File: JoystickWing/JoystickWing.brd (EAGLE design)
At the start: 32.7 x 69.8 mm, 14 parts, among them J1 5747844-4

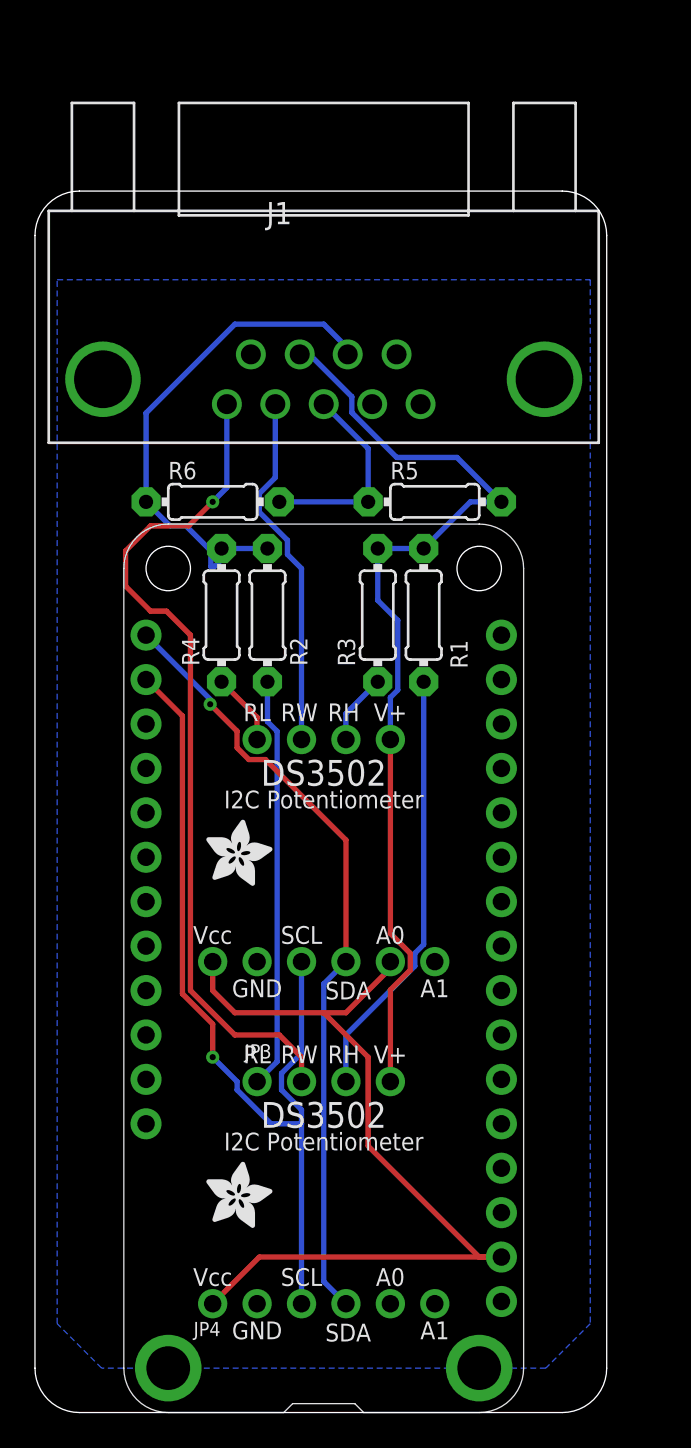
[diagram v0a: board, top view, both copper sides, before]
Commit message: Added NeoPixel w/jumper & pin
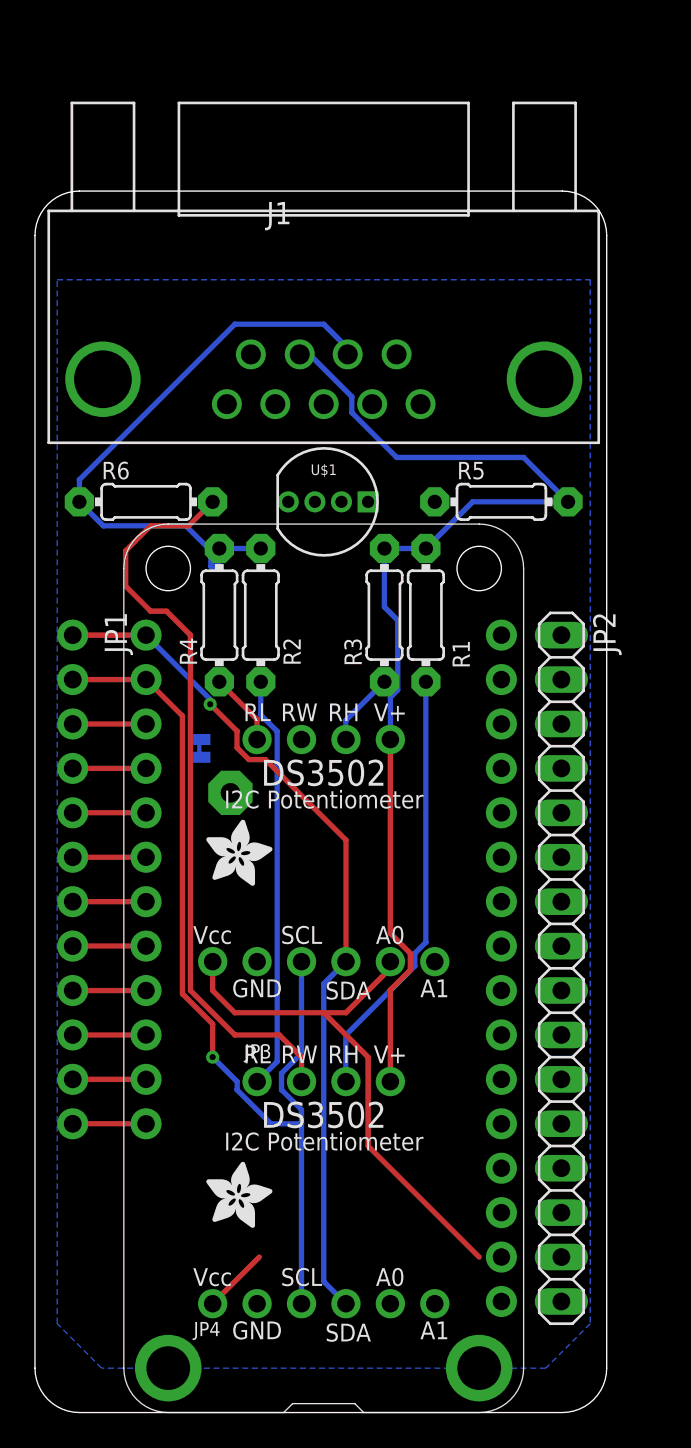
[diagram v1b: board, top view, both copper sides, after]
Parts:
- added JP1: (no value), adafruit:1X12-CB
- added JP2: (no value), pinhead:1X16
- added JP7: JUMPER-SMT_2_NC_TRACE_SILK, SparkFun-Jumpers:SMT-JUMPER_2_NC_TRACE_SILK
- added PAD1: (no value), wirepad:2,54/1,1
- added U$1: NEOPIXELS-5MM, milador:NEOPIXELS-5MM
- moved R5 3.81 mm to (26.7, 52.1)
- moved R6 3.81 mm to (6.35, 52.1)
- moved R2 0.38 mm to (12.9, 45.6)
- moved R3 0.38 mm to (20.0, 45.6)
- moved R1 0.13 mm to (22.4, 45.6)
- moved R4 0.13 mm to (10.5, 45.6)
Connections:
- new net N$1: JP1.3, JP7.1, MS1.19
- new net N$10: JP2.1, MS1.16
- new net N$11: JP2.2, MS1.15
- new net N$12: JP2.3, MS1.14
- new net N$13: JP2.4, MS1.13
- new net N$14: JP2.5, MS1.12
- new net N$15: JP2.6, MS1.11
- new net N$16: JP2.7, MS1.10
- new net N$17: JP2.8, MS1.9
- new net N$18: JP2.9, MS1.8
- new net N$19: JP2.10, MS1.7
- new net N$2: JP1.4, MS1.20
- new net N$20: JP2.11, MS1.6
- new net N$21: JP2.12, MS1.5
- new net N$22: JP2.13, MS1.4
- new net N$23: JP2.14, MS1.3
- new net N$24: JP2.16, MS1.1
- new net N$25: JP7.2, PAD1.1, U$1.1
- new net N$3: JP1.5, MS1.21
- new net N$4: JP1.6, MS1.22
- new net N$5: JP1.7, MS1.23
- new net N$6: JP1.8, MS1.24
- new net N$8: JP1.9, MS1.25
- new net N$9: JP1.11, MS1.27
- new net USB: JP1.10, MS1.26
- new net VBAT: JP1.12, MS1.28
- net GND: now also U$1.3; no longer MS1.4
- net SCL: now also JP1.2
- net SDA: now also JP1.1
- net VCC: now also JP2.15, U$1.2
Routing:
- net P2RW: track 20.6 -> 0.00 mm
- net VCC: track 50.3 -> 35.2 mm
- net N$7: track 11.7 -> 0.00 mm
- net +12V: track 55.8 -> 62.9 mm
- net P1RW: track 48.6 -> 42.7 mm
- net GND: track 29.2 -> 34.2 mm
- net SDA: track 44.6 -> 48.8 mm
- net SCL: track 50.6 -> 54.8 mm
- net VBAT: track 0.00 -> 4.19 mm
- net USB: track 0.00 -> 4.19 mm
- net N$9: track 0.00 -> 4.19 mm
- net N$8: track 0.00 -> 4.19 mm
- net N$6: track 0.00 -> 4.19 mm
- net N$5: track 0.00 -> 4.19 mm
- net N$4: track 0.00 -> 4.19 mm
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
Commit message: Updated to add neopixel & jumper - no air wires
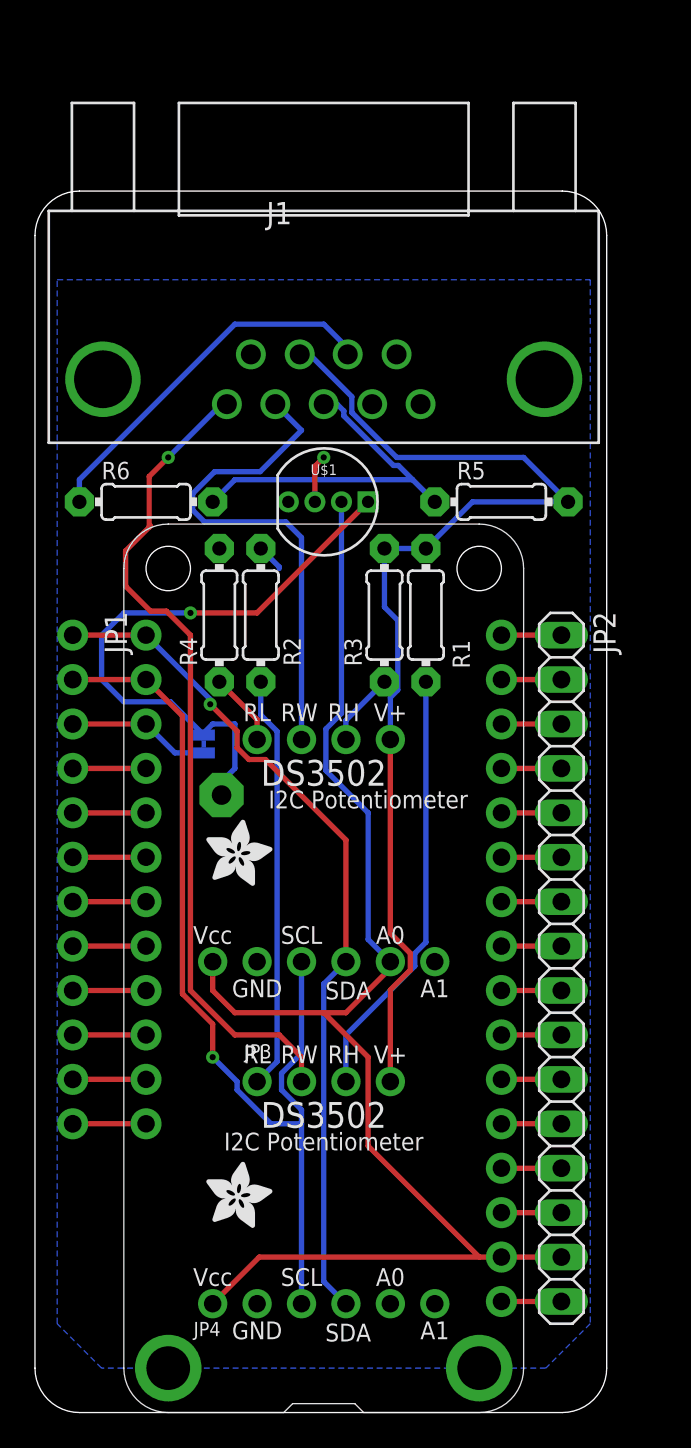
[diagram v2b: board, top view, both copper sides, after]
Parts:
- moved PAD1 0.52 mm to (10.7, 35.3)
- moved JP7 0.36 mm to (9.65, 38.2), turned to 90 degrees
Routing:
- net VCC: track 35.2 -> 80.6 mm
- net N$25: track 0.00 -> 34.6 mm, vias 0 -> 1
- net P2RW: track 0.00 -> 29.2 mm
- net N$7: track 0.00 -> 20.8 mm
- net GND: track 34.2 -> 25.5 mm, vias 0 -> 1
- net P1RW: track 42.7 -> 47.6 mm
- net N$1: track 4.19 -> 8.18 mm
- net N$18: track 0.00 -> 3.81 mm
- net N$17: track 0.00 -> 3.81 mm
- net N$24: track 0.00 -> 3.43 mm
- net N$23: track 0.00 -> 3.43 mm
- net N$22: track 0.00 -> 3.43 mm
- net N$21: track 0.00 -> 3.43 mm
- net N$20: track 0.00 -> 3.43 mm
- net N$19: track 0.00 -> 3.43 mm
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
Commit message: Added User Switch Output
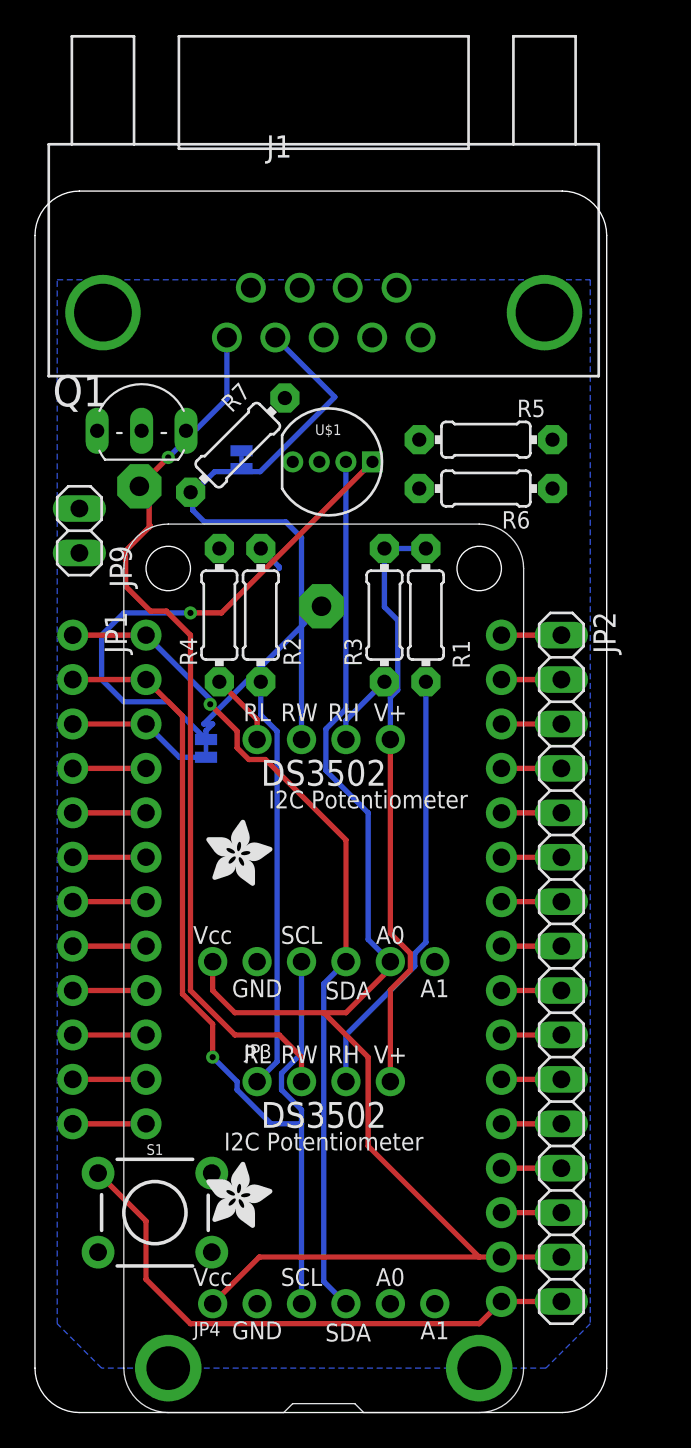
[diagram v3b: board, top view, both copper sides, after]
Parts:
- added JP8: JUMPER-SMT_2_NC_TRACE_SILK, SparkFun-Jumpers:SMT-JUMPER_2_NC_TRACE_SILK
- added JP9: (no value), pinhead:1X02
- added PAD2: (no value), wirepad:2,54/1,1
- added Q1: 2N2222, adafruit:TO92-EBC-OVAL
- added R7: 1K, adafruit:0204/7
- added S1: MOMENTARY-SWITCH-SPST-PTH-6.0MM, SparkFun-Switches:TACTILE_SWITCH_PTH_6.0MM
- moved R6 19.4 mm to (25.8, 52.8), turned to 180 degrees
- moved PAD1 12.2 mm to (16.4, 46.1)
- moved J1 3.81 mm to (16.5, 72.4)
- moved R5 3.67 mm to (25.8, 55.6)
- moved U$1 2.30 mm to (17.0, 54.4)
- moved JP7 0.28 mm to (9.78, 38.0)
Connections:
- removed net N$22: JP2.13, MS1.4
- new net N$26: Q1.B, R7.1
- new net N$27: JP9.1, Q1.E
- new net N$28: JP8.2, PAD2.1, R7.2
- net GND: now also JP2.13, JP9.2, MS1.4, S1.3
- net N$2: now also JP8.1
- net N$24: now also S1.1
- net N$7: now also Q1.C
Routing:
- net N$24: track 3.43 -> 32.5 mm
- net +12V: track 62.9 -> 34.3 mm
- net N$7: track 20.8 -> 0.00 mm
- net GND: track 25.5 -> 5.01 mm, vias 1 -> 0
- net N$25: track 34.6 -> 40.6 mm
- net P2RW: track 29.2 -> 34.6 mm
- net P1RW: track 47.6 -> 51.2 mm
- net N$22: track 3.43 -> 0.00 mm
- net VCC: track 80.6 -> 83.0 mm

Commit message: Removed transistor
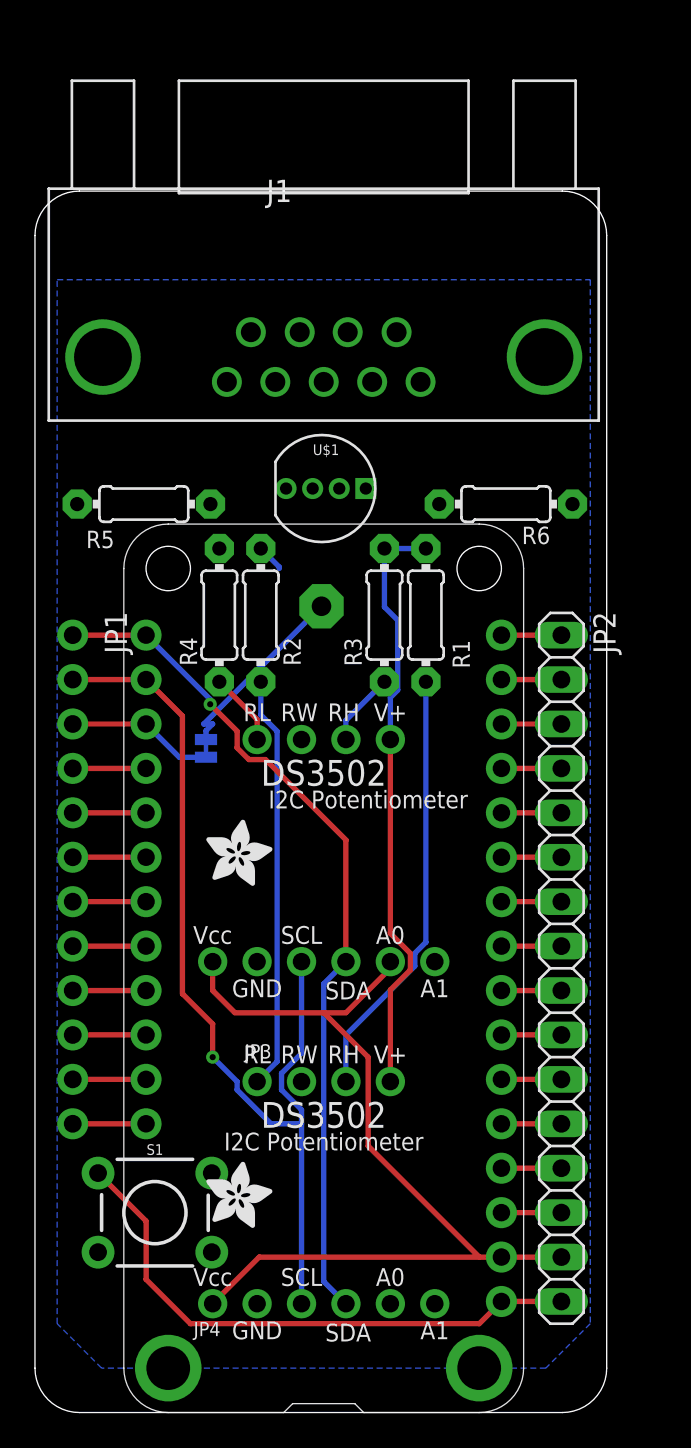
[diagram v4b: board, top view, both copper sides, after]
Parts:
- removed JP8: JUMPER-SMT_2_NC_TRACE_SILK, SparkFun-Jumpers:SMT-JUMPER_2_NC_TRACE_SILK
- removed JP9: (no value), pinhead:1X02
- removed PAD2: (no value), wirepad:2,54/1,1
- removed Q1: 2N2222, adafruit:TO92-EBC-OVAL
- removed R7: 1K, adafruit:0204/7
- moved R5 19.9 mm to (6.22, 51.9)
- moved J1 2.54 mm to (16.5, 69.8)
- moved U$1 1.57 mm to (16.6, 52.8)
- moved R6 1.45 mm to (26.9, 51.9)
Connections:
- removed net N$26: Q1.B, R7.1
- removed net N$27: JP9.1, Q1.E
- removed net N$28: JP8.2, PAD2.1, R7.2
- net GND: no longer JP9.2
- net N$2: no longer JP8.1
- net N$7: no longer Q1.C
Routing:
- net P1RW: track 51.2 -> 0.00 mm, vias 1 -> 0
- net P2RW: track 34.6 -> 0.00 mm
- net VCC: track 83.0 -> 52.5 mm
- net N$25: track 40.6 -> 11.1 mm, vias 1 -> 0

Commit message: No AirWires & ready for reset button and double check
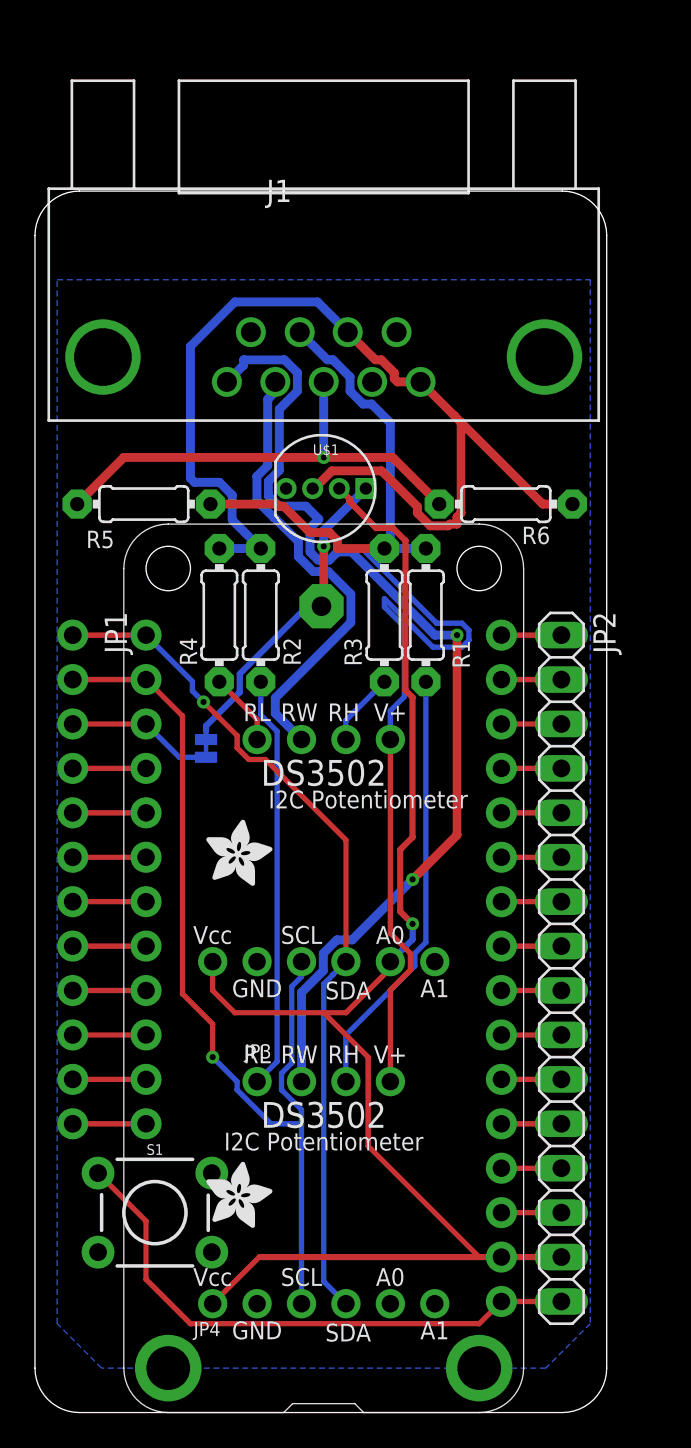
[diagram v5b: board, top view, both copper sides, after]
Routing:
- net GND: track 5.01 -> 63.8 mm
- net P1RW: track 0.00 -> 58.8 mm, vias 0 -> 2
- net +12V: track 34.3 -> 74.2 mm
- net VCC: track 52.5 -> 82.9 mm, vias 0 -> 1
- net N$7: track 0.00 -> 27.2 mm, vias 0 -> 1
- net P2RW: track 0.00 -> 26.0 mm
- net N$25: track 11.1 -> 18.6 mm, vias 0 -> 1

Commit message: Update with address pads
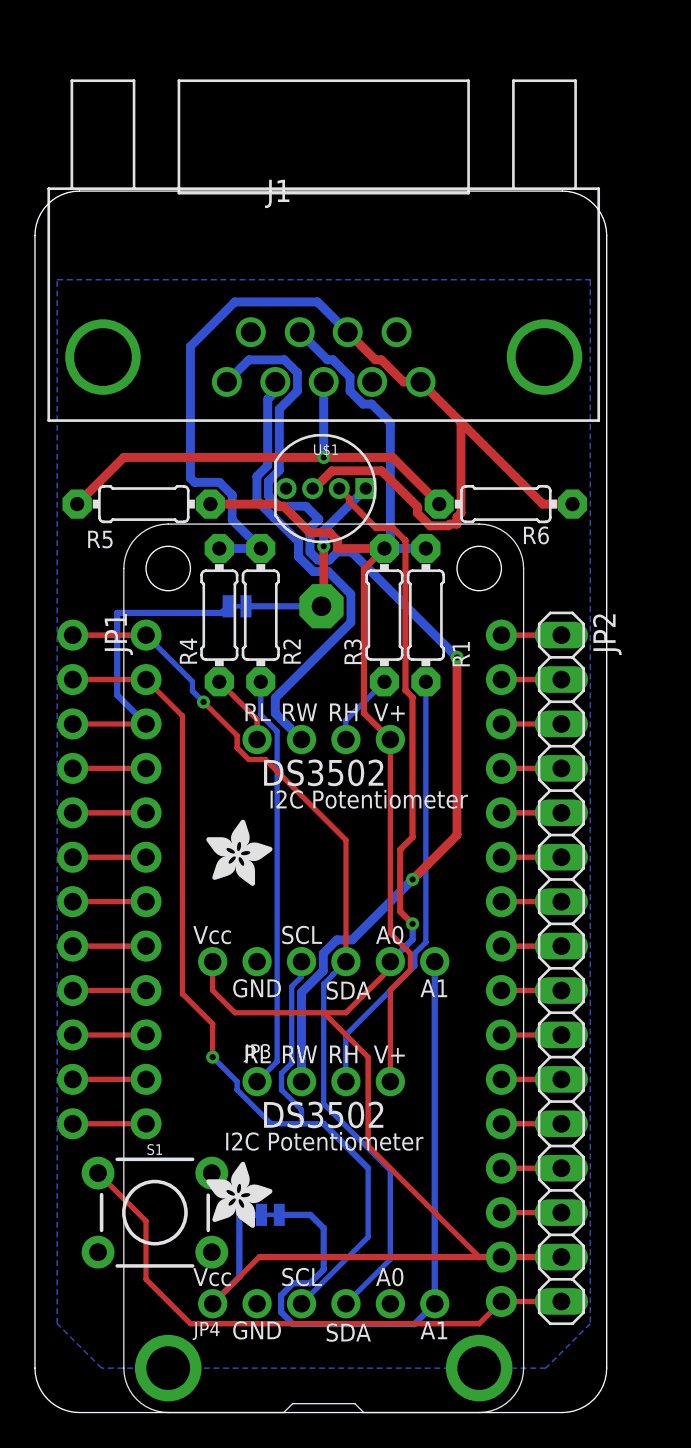
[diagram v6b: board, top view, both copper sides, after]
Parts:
- added A1: JUMPER-SMT_2_NC_TRACE_SILK, SparkFun-Jumpers:SMT-JUMPER_2_NC_TRACE_SILK
- moved JP7 8.32 mm to (11.6, 46.1), turned to 180 degrees
- renumbered PAD1 to NEOPIN
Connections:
- removed net P1A1: JP4.6
- removed net P2A1: JP6.6
- new net ADDR: A1.1, JP4.6, JP6.6
- net VCC: now also A1.2
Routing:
- net ADDR: track 0.00 -> 38.6 mm
- net +12V: track 74.2 -> 61.3 mm
- net N$1: track 8.41 -> 17.7 mm
- net VCC: track 82.9 -> 89.9 mm
- net N$25: track 18.6 -> 12.1 mm
- net SCL: track 54.8 -> 58.7 mm
- net SDA: track 48.8 -> 50.9 mm
- net P1RW: track 58.8 -> 57.8 mm
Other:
- board text added: "3V"
- board text added: "JoyStick"
- board text added: "Uncut = 1 Cut = 0"

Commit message: Added the missing Neopixel led pads and updated the switch to DTS-3: 3.5x6mm style switch.
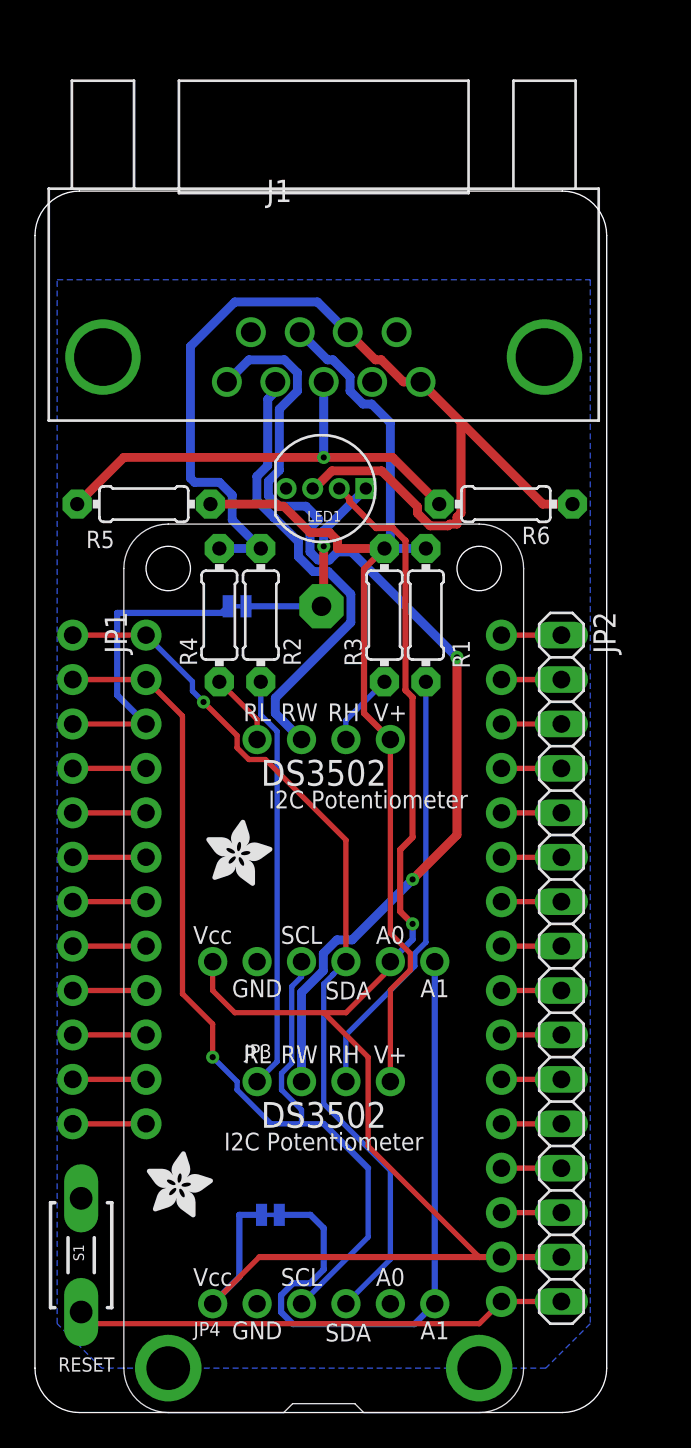
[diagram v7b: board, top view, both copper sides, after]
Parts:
- S1: value MOMENTARY-SWITCH-SPST-PTH-6.0MM -> RESET; device SparkFun-Switches:TACTILE_SWITCH_PTH_6.0MM -> milador:DTS-3
- moved S1 4.87 mm to (2.64, 9.00), turned to 90 degrees
- moved U$10 3.45 mm to (6.38, 11.1)
- renumbered U$1 to LED1
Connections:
- net GND: now also LED1.P3, S1.2; no longer LED1.3, S1.3
- net N$25: now also LED1.P1; no longer LED1.1
- net VCC: now also LED1.P2; no longer LED1.2
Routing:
- net N$24: track 32.5 -> 28.3 mm
